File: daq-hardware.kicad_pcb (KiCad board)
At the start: 4 copper layers, 100 x 60 mm, 98 parts, among them J1 USB_B, J10 Screw_Terminal_01x02, J11 Screw_Terminal_01x01, J12 Screw_Terminal_01x01, J13 Screw_Terminal_01x01, J14 Screw_Terminal_01x01, J2 Micro_SD_Card_Det_Hirose_DM3AT, J3 Conn_01x02, J4 Screw_Terminal_01x02, J5 Screw_Terminal_Thermo_1, J6 Screw_Terminal_Thermo_2, J7 Screw_Terminal_Thermo_3, J8 Screw_Terminal_Thermo_4, J9 Screw_Terminal_01x02, Q1 MMDT2222A, Q2 PMV20ENR, U1 CP2102N-A01-GQFN24, U10 LTV-817S, U11 ADS131M04, U2 ESP32-WROOM-32D, U3 TPS61093, U4 TPS62160DGK, U5 TPS62160DGK, U6 MAX31855RASA, U7 MAX31855RASA, U8 MAX31855RASA, U9 MAX31855RASA

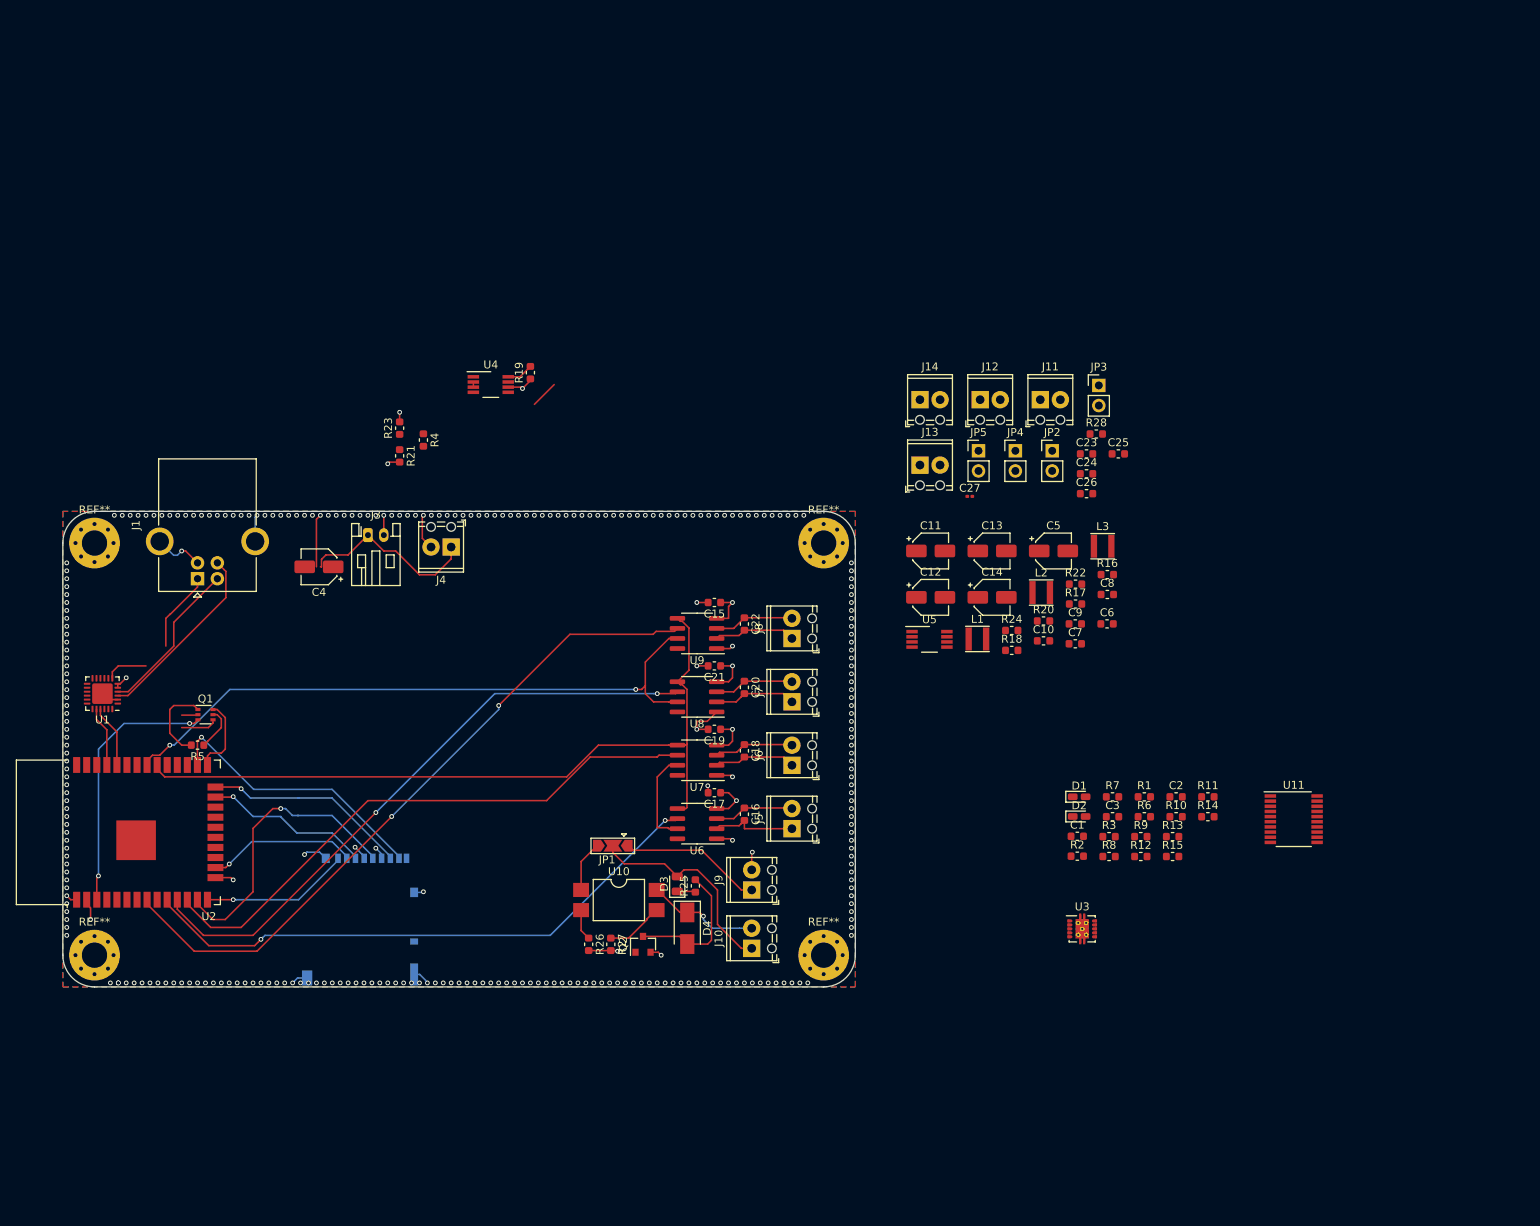
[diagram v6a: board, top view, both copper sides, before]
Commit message: Cleaned up layout, added barrel jack for power input
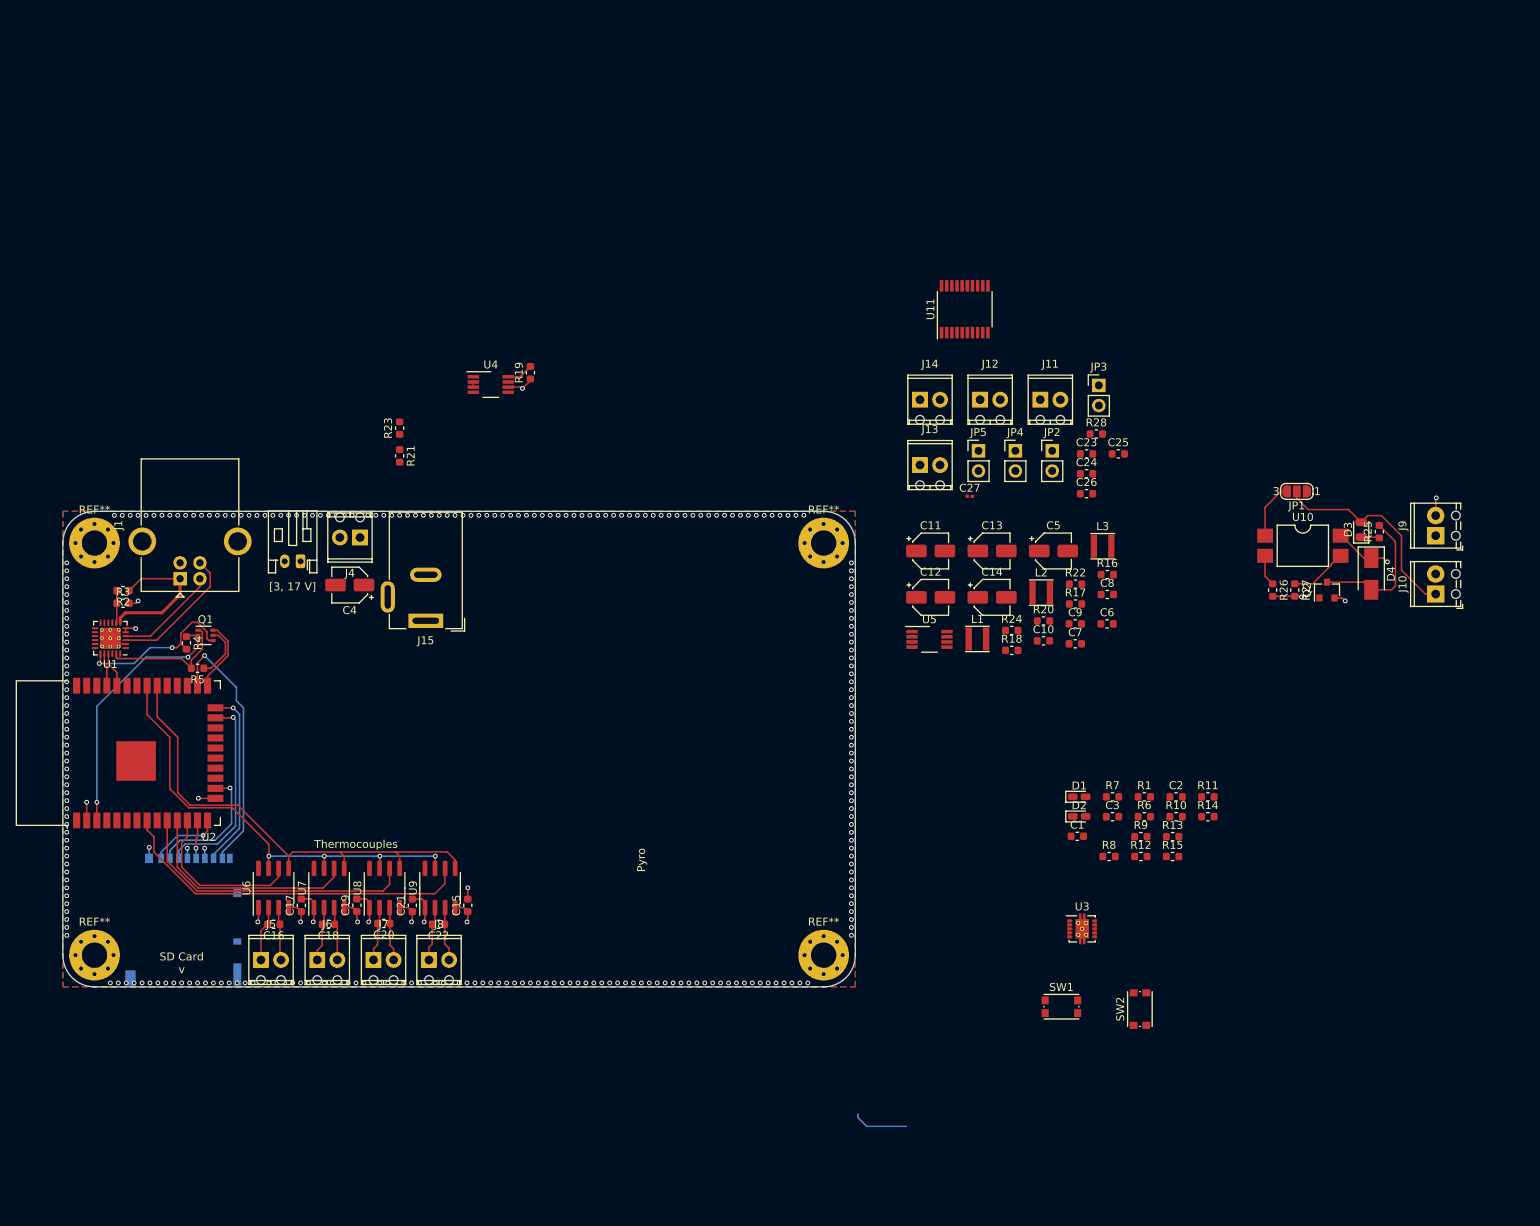
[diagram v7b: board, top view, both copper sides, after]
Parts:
- added J15: Barrel_Jack_Switch, Connector_BarrelJack:BarrelJack_Wuerth_6941xx301002, F.Cu at (145.8, 93.8)
- added SW1: SW1, Button_Switch_SMD:SW_Push_1P1T_NO_CK_KMR2, F.Cu at (226.0, 142.5)
- added SW2: SW1, Button_Switch_SMD:SW_Push_1P1T_NO_CK_KMR2, F.Cu at (235.9, 142.8)
- J11, J12, J13, J14, J4, J5, J6, J7, J8: footprint TerminalBlock_Phoenix:TerminalBlock_Phoenix_MPT-0,5-2-2.54_1x02_P2.54mm_Horizontal -> TerminalBlock_Phoenix:TerminalBlock_Phoenix_MPT-2.54mm_2pol
- JP1: footprint Jumper:SolderJumper-3_P2.0mm_Open_TrianglePad1.0x1.5mm -> Jumper:SolderJumper-3_P1.3mm_Open_RoundedPad1.0x1.5mm_NumberLabels
- U1: footprint Package_DFN_QFN:QFN-24-1EP_4x4mm_P0.5mm_EP2.6x2.6mm -> Package_DFN_QFN:QFN-24-1EP_4x4mm_P0.5mm_EP2.6x2.6mm_ThermalVias
- moved R3 127.8 mm to (107.6, 91.6)
- moved R2 125.0 mm to (107.6, 90.0), turned to 180 degrees
- moved D3 97.2 mm to (263.8, 82.3)
- moved D4 97.2 mm to (265.1, 87.9)
- moved JP1 97.2 mm to (255.7, 77.5)
- moved R25 97.2 mm to (266.1, 82.6)
- moved R26 97.2 mm to (252.7, 89.9)
- moved J10 97.2 mm to (273.2, 90.4)
- moved J9 97.2 mm to (273.2, 83.1)
- moved Q2 97.2 mm to (259.5, 89.9)
- moved R27 97.2 mm to (255.4, 89.9)
- moved U10 97.2 mm to (256.5, 84.3)
- moved U11 76.6 mm to (213.8, 54.5), turned to 90 degrees
- moved J5 69.0 mm to (125.0, 136.6), turned to 0 degrees
- moved J6 64.7 mm to (132.1, 136.6), turned to 0 degrees
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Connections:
- U2 pad 10: /~TC_CS1 -> /~TC_CS3
- U2 pad 12: /~TC_CS3 -> /~TC_CS1
- U7 pad 6: /~TC_CS3 -> /~TC_CS2
- U8 pad 6: /~TC_CS2 -> /~TC_CS3
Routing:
- net /~TC_CS1: track 73.7 -> 21.2 mm, vias 2 -> 0
- net /~TC_CS2: track 78.4 -> 28.4 mm, vias 2 -> 0
- net /~TC_CS4: track 87.1 -> 45.7 mm, vias 2 -> 0
- net /~TC_CS3: track 72.6 -> 37.1 mm
- net /SCLK: track 96.6 -> 61.6 mm
- net /MISO: track 93.2 -> 58.3 mm, vias 2 -> 4
- net /SD_CLK: track 36.9 -> 4.87 mm
- net GND: track 62.7 -> 31.2 mm, vias 289 -> 271
- net VDD: track 23.8 -> 0.65 mm
- net Net-(J10-Pad1): track 17.8 -> 0.00 mm
- net /RTS: track 4.59 -> 21.0 mm, vias 0 -> 2
- net +3V3: track 39.0 -> 28.7 mm, vias 9 -> 8
- net /SD_D2: track 18.8 -> 9.06 mm
- net Net-(J1-Pad2): track 20.2 -> 13.0 mm
- net Net-(J1-Pad3): track 23.6 -> 17.0 mm
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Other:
- board text added: "Pyro"
- board text added: "SD Card v"
- board text added: "Thermocouples"
- board text added: "[3, 17 V]"

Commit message: Laid out +3V3 section
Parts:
- added C28: 2.2n, Capacitor_SMD:C_0603_1608Metric, F.Cu at (131.5, 91.4)
- added D5: D_Schottky, Diode_SMD:D_SOD-123F, F.Cu at (128.3, 93.6)
- added D6: D_Schottky, Diode_SMD:D_SOD-123F, F.Cu at (138.3, 93.5)
- added Q3: PMV20ENR, Package_TO_SOT_SMD:SOT-23, F.Cu at (131.5, 94.0)
- added U13: TPS2412PW, Package_SO:TSSOP-8_4.4x3mm_P0.65mm, F.Cu at (135.2, 91.7)
- moved L2 88.4 mm to (135.4, 98.1), turned to 90 degrees
- moved C5 81.6 mm to (144.8, 100.2), turned to 270 degrees
- moved C11 71.3 mm to (139.8, 100.2), turned to 270 degrees
- moved C13 69.1 mm to (149.8, 100.2), turned to 270 degrees
- moved R19 43.8 mm to (132.0, 97.0), turned to 180 degrees
- moved U4 42.8 mm to (130.2, 99.6)
- moved R23 34.3 mm to (132.2, 102.2), turned to 0 degrees
- moved SW1 30.5 mm to (205.0, 164.6), turned to 180 degrees
- moved R21 29.5 mm to (134.4, 101.4), turned to 90 degrees
- moved C4 12.9 mm to (124.3, 94.3), turned to 90 degrees
- moved C6 11.7 mm to (240.4, 102.1)
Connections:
- J15 pad 1: VDD -> VCC
- J3 pad 1: VDD -> +BATT
- J4 pad 1: VDD -> VCC
- R6 pad 2: /GPIO0 -> (no net)
- R8 pad 1: /GPIO0 -> /BOOT
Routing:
- net VBUS: track 18.4 -> 43.4 mm
- net VCC: track 0.00 -> 17.9 mm
- net +BATT: track 0.00 -> 13.5 mm
- net VDD: track 0.65 -> 9.51 mm
- net Net-(Q3-Pad1): track 0.00 -> 8.04 mm
- net Net-(D4-Pad1): track 14.2 -> 7.27 mm
- net +3V3: track 28.7 -> 33.8 mm, vias 8 -> 7
- net GND: track 31.2 -> 35.5 mm, vias 271 -> 274
- net Net-(C28-Pad1): track 0.00 -> 4.06 mm
- net Net-(R21-Pad1): track 0.00 -> 3.29 mm
- net /power/PG: track 3.34 -> 2.66 mm
- added copper zone on F.Cu, net +3V3
- added copper zone on F.Cu, net Net-(L2-Pad1)
- added copper zone on F.Cu, net VDD
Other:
- board text added: "[3, 15 V]"
- board text removed: "[3, 17 V]"
